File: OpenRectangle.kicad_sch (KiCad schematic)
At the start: 51 parts, among them J1 USB C Connector, J2 JTAG_TC2030, SW1 Boot, U1 XC6206, U2 USBLC6-2SC6, U3 RP2040, U4 W25Q128JVS, Y1 12MHz

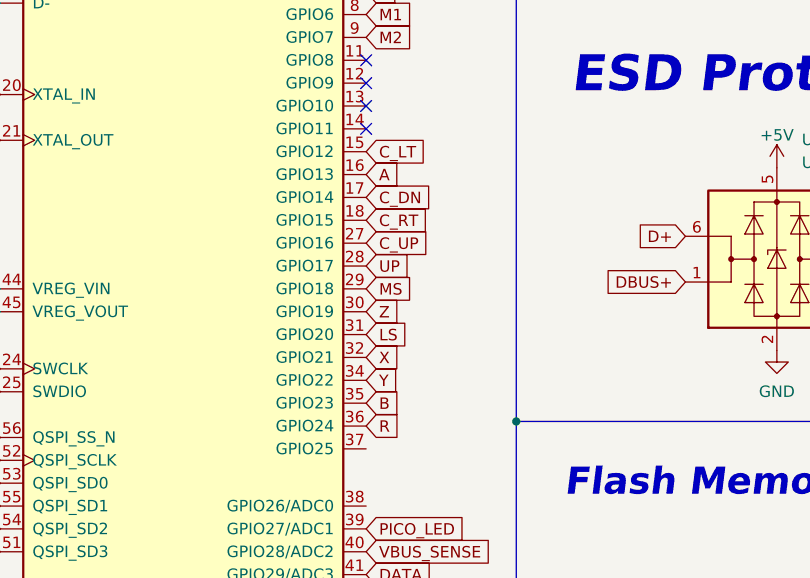
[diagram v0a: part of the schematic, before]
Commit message: modified OpenRectangle design
Modified OpenRectangle design to make it smaller and change button positions
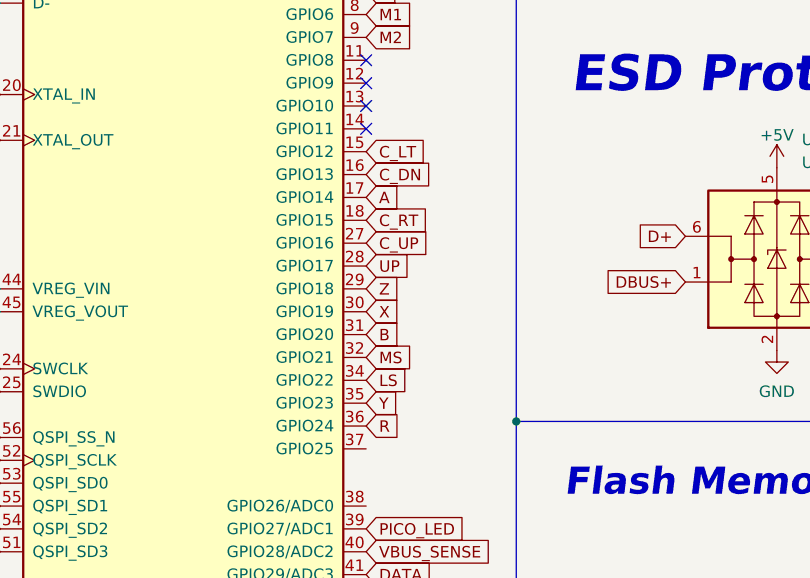
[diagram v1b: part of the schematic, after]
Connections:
- net A: now also U3.17 (GPIO14); no longer U3.16 (GPIO13)
- net B: now also U3.31 (GPIO20); no longer U3.35 (GPIO23)
- net C_DN: now also U3.16 (GPIO13); no longer U3.17 (GPIO14)
- net LS: now also U3.34 (GPIO22); no longer U3.31 (GPIO20)
- net MS: now also U3.32 (GPIO21); no longer U3.29 (GPIO18)
- net X: now also U3.30 (GPIO19); no longer U3.32 (GPIO21)
- net Y: now also U3.35 (GPIO23); no longer U3.34 (GPIO22)
- net Z: now also U3.29 (GPIO18); no longer U3.30 (GPIO19)
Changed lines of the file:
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@@
     )
   )
-  (global_label "Y" (shape input) (at 71.9648 104.394 0) (fields_autoplaced)
-    (effects (font (size 1.27 1.27)) (justify left))
-    (property "Intersheetrefs" "${INTERSHEET_REFS}" (at 75.4665 104.3146 0)
+  (global_label "Y" (shape input) (at 71.9648 106.934 0) (fields_autoplaced)
+    (effects (font (size 1.27 1.27)) (justify left))
+    (property "Intersheetrefs" "${INTERSHEET_REFS}" (at 75.4665 106.8546 0)
       (effects (font (size 1.27 1.27)) (justify left) hide)
     )
@@
     )
   )
-  (global_label "C_DN" (shape input) (at 71.9648 84.074 0) (fields_autoplaced)
-    (effects (font (size 1.27 1.27)) (justify left))
-    (property "Intersheetrefs" "${INTERSHEET_REFS}" (at 79.216 83.9946 0)
+  (global_label "C_DN" (shape input) (at 71.9648 81.534 0) (fields_autoplaced)
+    (effects (font (size 1.27 1.27)) (justify left))
+    (property "Intersheetrefs" "${INTERSHEET_REFS}" (at 79.216 81.4546 0)
       (effects (font (size 1.27 1.27)) (justify left) hide)
     )
@@
     )
   )
-  (global_label "Z" (shape input) (at 71.9648 96.774 0) (fields_autoplaced)
+  (global_label "Z" (shape input) (at 71.9648 94.234 0) (fields_autoplaced)
+    (effects (font (size 1.27 1.27)) (justify left))
+    (property "Intersheetrefs" "${INTERSHEET_REFS}" (at 75.5874 94.1546 0)
+      (effects (font (size 1.27 1.27)) (justify left) hide)
+    )
+  )
+  (global_label "~{RESET}" (shape input) (at 25.8891 48.514 180) (fields_autoplaced)
+    (effects (font (size 1.27 1.27)) (justify right))
+    (property "Intersheetrefs" "${INTERSHEET_REFS}" (at 17.7308 48.4346 0)
+      (effects (font (size 1.27 1.27)) (justify right) hide)
+    )
+  )
+  (global_label "~{RESET}" (shape input) (at 155.702 177.546 180) (fields_autoplaced)
+    (effects (font (size 1.27 1.27)) (justify right))
+    (property "Intersheetrefs" "${INTERSHEET_REFS}" (at 147.5437 177.6254 0)
+      (effects (font (size 1.27 1.27)) (justify right) hide)
+    )
+  )
+  (global_label "XTAL_OUT" (shape input) (at 31.3248 77.724 180) (fields_autoplaced)
+    (effects (font (size 1.27 1.27)) (justify right))
+    (property "Intersheetrefs" "${INTERSHEET_REFS}" (at 20.0217 77.6446 0)
+      (effects (font (size 1.27 1.27)) (justify right) hide)
+    )
+  )
+  (global_label "SD1" (shape input) (at 31.3248 118.364 180) (fields_autoplaced)
+    (effects (font (size 1.27 1.27)) (justify right))
+    (property "Intersheetrefs" "${INTERSHEET_REFS}" (at 25.2227 118.2846 0)
+      (effects (font (size 1.27 1.27)) (justify right) hide)
+    )
+  )
+  (global_label "VBUS_SENSE" (shape input) (at 207.5942 151.384 0) (fields_autoplaced)
+    (effects (font (size 1.27 1.27)) (justify left))
+    (property "Intersheetrefs" "${INTERSHEET_REFS}" (at 222.4137 151.384 0)
+      (effects (font (size 1.27 1.27)) (justify left) hide)
+    )
+  )
+  (global_label "SWCLK" (shape input) (at 155.702 180.086 180) (fields_autoplaced)
+    (effects (font (size 1.27 1.27)) (justify right))
+    (property "Intersheetrefs" "${INTERSHEET_REFS}" (at 147.0599 180.1654 0)
+      (effects (font (size 1.27 1.27)) (justify right) hide)
+    )
+  )
+  (global_label "X" (shape input) (at 71.9648 96.774 0) (fields_autoplaced)
     (effects (font (size 1.27 1.27)) (justify left))
     (property "Intersheetrefs" "${INTERSHEET_REFS}" (at 75.5874 96.6946 0)
@@
     )
   )
-  (global_label "~{RESET}" (shape input) (at 25.8891 48.514 180) (fields_autoplaced)
-    (effects (font (size 1.27 1.27)) (justify right))
-    (property "Intersheetrefs" "${INTERSHEET_REFS}" (at 17.7308 48.4346 0)
-      (effects (font (size 1.27 1.27)) (justify right) hide)
-    )
-  )
-  (global_label "~{RESET}" (shape input) (at 155.702 177.546 180) (fields_autoplaced)
-    (effects (font (size 1.27 1.27)) (justify right))
-    (property "Intersheetrefs" "${INTERSHEET_REFS}" (at 147.5437 177.6254 0)
-      (effects (font (size 1.27 1.27)) (justify right) hide)
-    )
-  )
-  (global_label "XTAL_OUT" (shape input) (at 31.3248 77.724 180) (fields_autoplaced)
-    (effects (font (size 1.27 1.27)) (justify right))
-    (property "Intersheetrefs" "${INTERSHEET_REFS}" (at 20.0217 77.6446 0)
-      (effects (font (size 1.27 1.27)) (justify right) hide)
-    )
-  )
-  (global_label "SD1" (shape input) (at 31.3248 118.364 180) (fields_autoplaced)
-    (effects (font (size 1.27 1.27)) (justify right))
-    (property "Intersheetrefs" "${INTERSHEET_REFS}" (at 25.2227 118.2846 0)
-      (effects (font (size 1.27 1.27)) (justify right) hide)
-    )
-  )
-  (global_label "VBUS_SENSE" (shape input) (at 207.5942 151.384 0) (fields_autoplaced)
-    (effects (font (size 1.27 1.27)) (justify left))
-    (property "Intersheetrefs" "${INTERSHEET_REFS}" (at 222.4137 151.384 0)
-      (effects (font (size 1.27 1.27)) (justify left) hide)
-    )
-  )
-  (global_label "SWCLK" (shape input) (at 155.702 180.086 180) (fields_autoplaced)
-    (effects (font (size 1.27 1.27)) (justify right))
-    (property "Intersheetrefs" "${INTERSHEET_REFS}" (at 147.0599 180.1654 0)
-      (effects (font (size 1.27 1.27)) (justify right) hide)
-    )
-  )
-  (global_label "X" (shape input) (at 71.9648 101.854 0) (fields_autoplaced)
-    (effects (font (size 1.27 1.27)) (justify left))
-    (property "Intersheetrefs" "${INTERSHEET_REFS}" (at 75.5874 101.7746 0)
-      (effects (font (size 1.27 1.27)) (justify left) hide)
-    )
-  )
-  (global_label "A" (shape input) (at 71.9648 81.534 0) (fields_autoplaced)
-    (effects (font (size 1.27 1.27)) (justify left))
-    (property "Intersheetrefs" "${INTERSHEET_REFS}" (at 75.4665 81.4546 0)
+  (global_label "A" (shape input) (at 71.9648 84.074 0) (fields_autoplaced)
+    (effects (font (size 1.27 1.27)) (justify left))
+    (property "Intersheetrefs" "${INTERSHEET_REFS}" (at 75.4665 83.9946 0)
       (effects (font (size 1.27 1.27)) (justify left) hide)
     )
@@
     )
   )
-  (global_label "LS" (shape input) (at 71.9648 99.314 0) (fields_autoplaced)
-    (effects (font (size 1.27 1.27)) (justify left))
-    (property "Intersheetrefs" "${INTERSHEET_REFS}" (at 76.6155 99.2346 0)
+  (global_label "LS" (shape input) (at 71.9648 104.394 0) (fields_autoplaced)
+    (effects (font (size 1.27 1.27)) (justify left))
+    (property "Intersheetrefs" "${INTERSHEET_REFS}" (at 76.6155 104.3146 0)
       (effects (font (size 1.27 1.27)) (justify left) hide)
     )
@@
     )
   )
-  (global_label "MS" (shape input) (at 71.9648 94.234 0) (fields_autoplaced)
-    (effects (font (size 1.27 1.27)) (justify left))
-    (property "Intersheetrefs" "${INTERSHEET_REFS}" (at 77.0389 94.1546 0)
+  (global_label "MS" (shape input) (at 71.9648 101.854 0) (fields_autoplaced)
+    (effects (font (size 1.27 1.27)) (justify left))
+    (property "Intersheetrefs" "${INTERSHEET_REFS}" (at 77.0389 101.7746 0)
       (effects (font (size 1.27 1.27)) (justify left) hide)
     )
@@
     )
   )
-  (global_label "B" (shape input) (at 71.9648 106.934 0) (fields_autoplaced)
-    (effects (font (size 1.27 1.27)) (justify left))
-    (property "Intersheetrefs" "${INTERSHEET_REFS}" (at 75.6479 106.8546 0)
-      (effects (font (size 1.27 1.27)) (justify left) hide)
-    )
+  (global_label "B" (shape input) (at 71.9648 99.314 0) (fields_autoplaced)
+    (effects (font (size 1.27 1.27)) (justify left))
+    (property "Intersheetrefs" "${INTERSHEET_REFS}" (at 75.6479 99.2346 0)
+      (effects (font (size 1.27 1.27)) (justify left) hide)
+    )

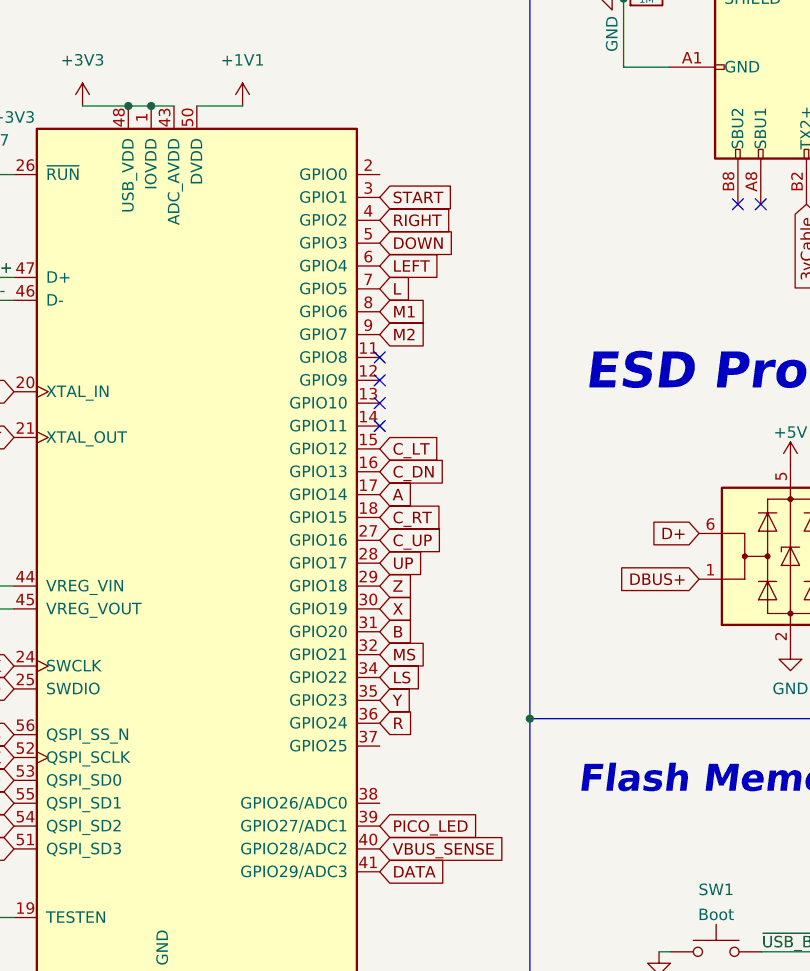
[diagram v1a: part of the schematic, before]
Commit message: Added optional buttons
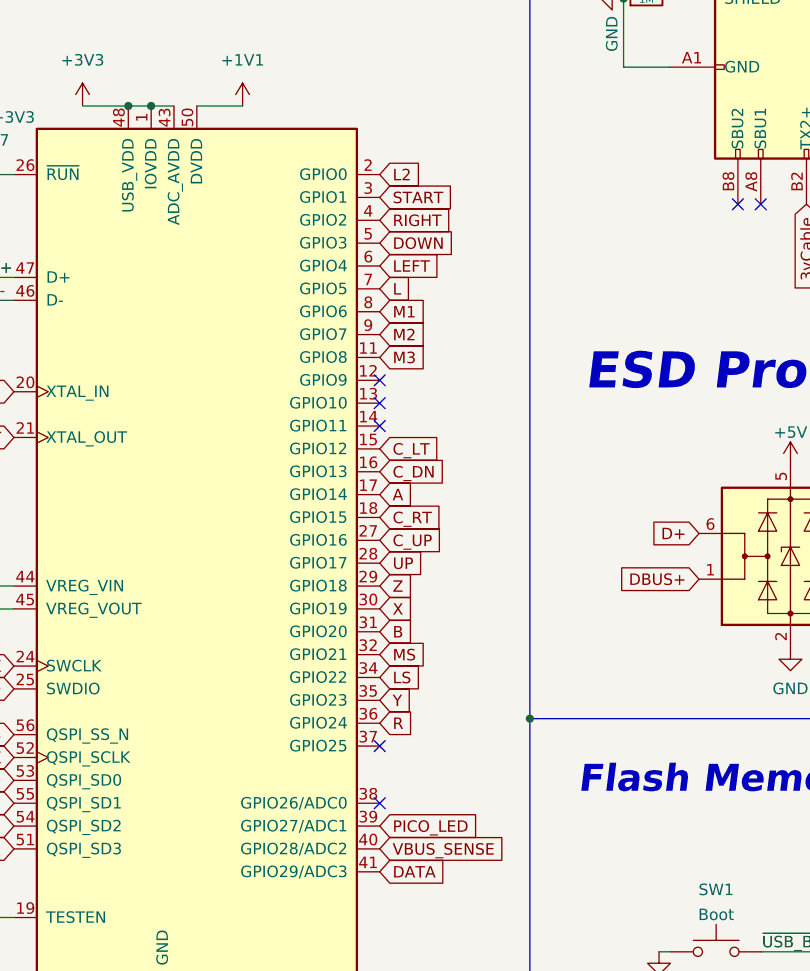
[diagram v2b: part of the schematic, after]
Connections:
- net M3: now reaches U3.11 (GPIO8)
- net L2: now reaches U3.2 (GPIO0)
- no-connect marks 9 -> 10
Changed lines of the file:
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@@
   (junction (at 65.786 180.34) (diameter 0) (color 0 0 0 0)
   )
-  (no_connect (at 71.9648 68.834))
+  (no_connect (at 71.9648 118.364))
+  (no_connect (at 71.9648 112.014))
   (no_connect (at 71.9648 71.374))
   (no_connect (at 71.9648 73.914))
@@
     )
   )
+  (global_label "L2" (shape input) (at 71.9648 48.514 0) (fields_autoplaced)
+    (effects (font (size 1.27 1.27)) (justify left))
+    (property "Intersheetrefs" "${INTERSHEET_REFS}" (at 77.1082 48.514 0)
+      (effects (font (size 1.27 1.27)) (justify left) hide)
+    )
+  )
   (global_label "C_DN" (shape input) (at 71.9648 81.534 0) (fields_autoplaced)
     (effects (font (size 1.27 1.27)) (justify left))
@@
     )
   )
+  (global_label "M3" (shape input) (at 71.9648 68.834 0) (fields_autoplaced)
+    (effects (font (size 1.27 1.27)) (justify left))
+    (property "Intersheetrefs" "${INTERSHEET_REFS}" (at 77.5315 68.834 0)
+      (effects (font (size 1.27 1.27)) (justify left) hide)
+    )
+  )

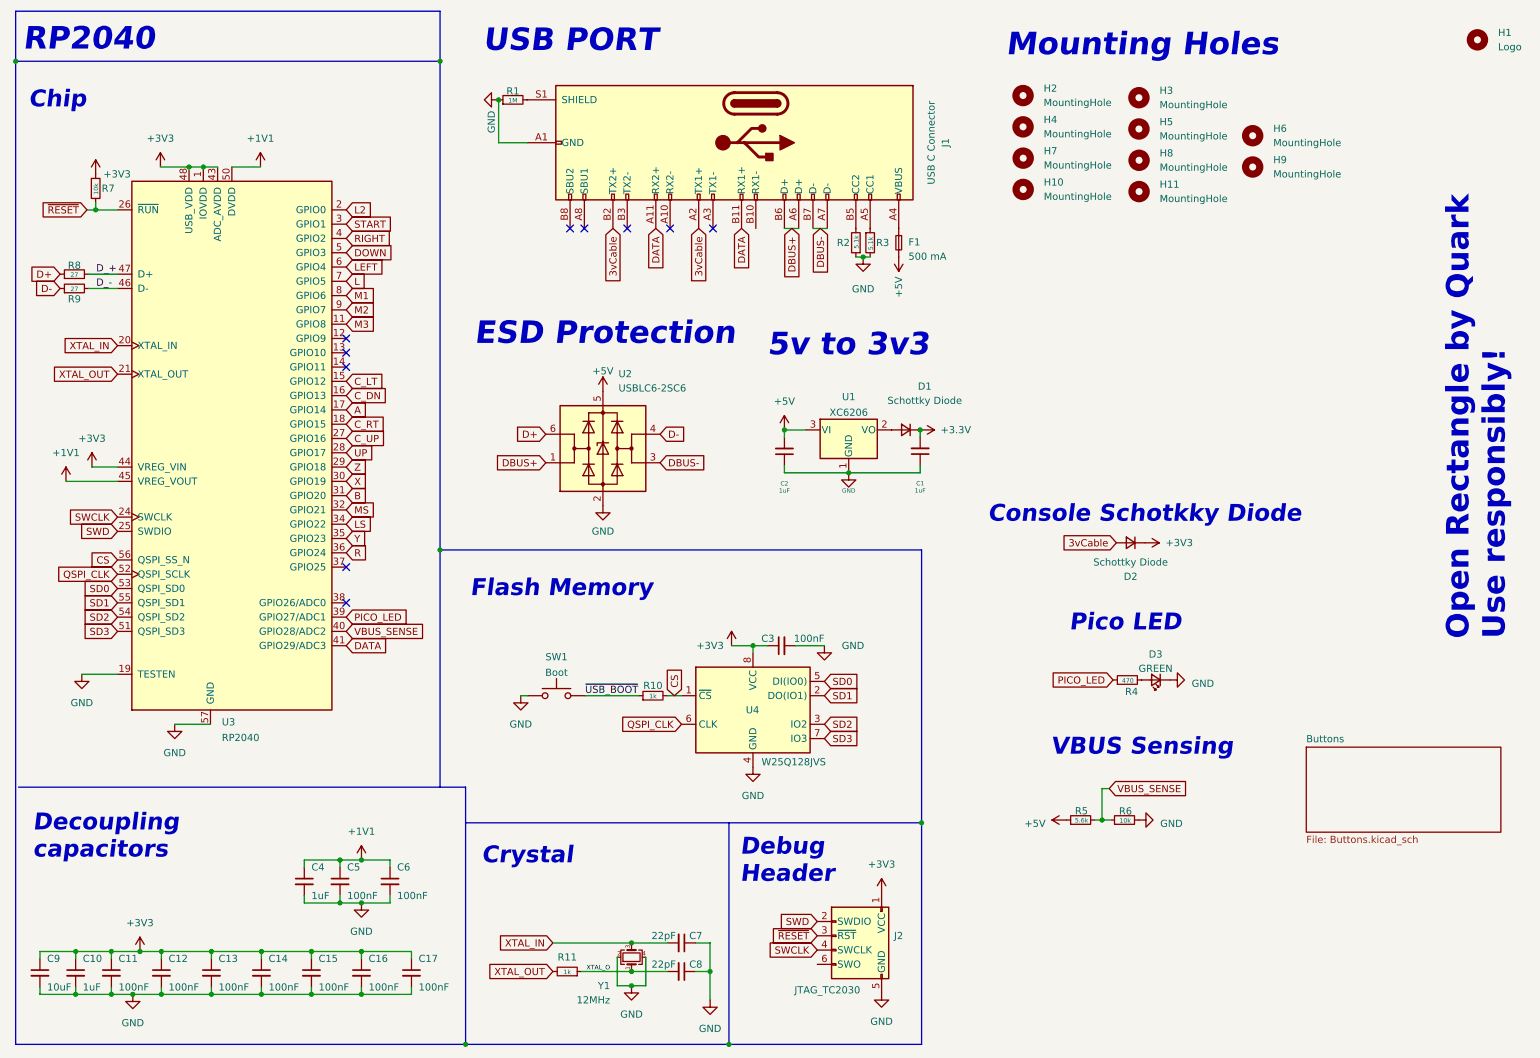
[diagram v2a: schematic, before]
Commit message: updated pinout to default haybox and revised case
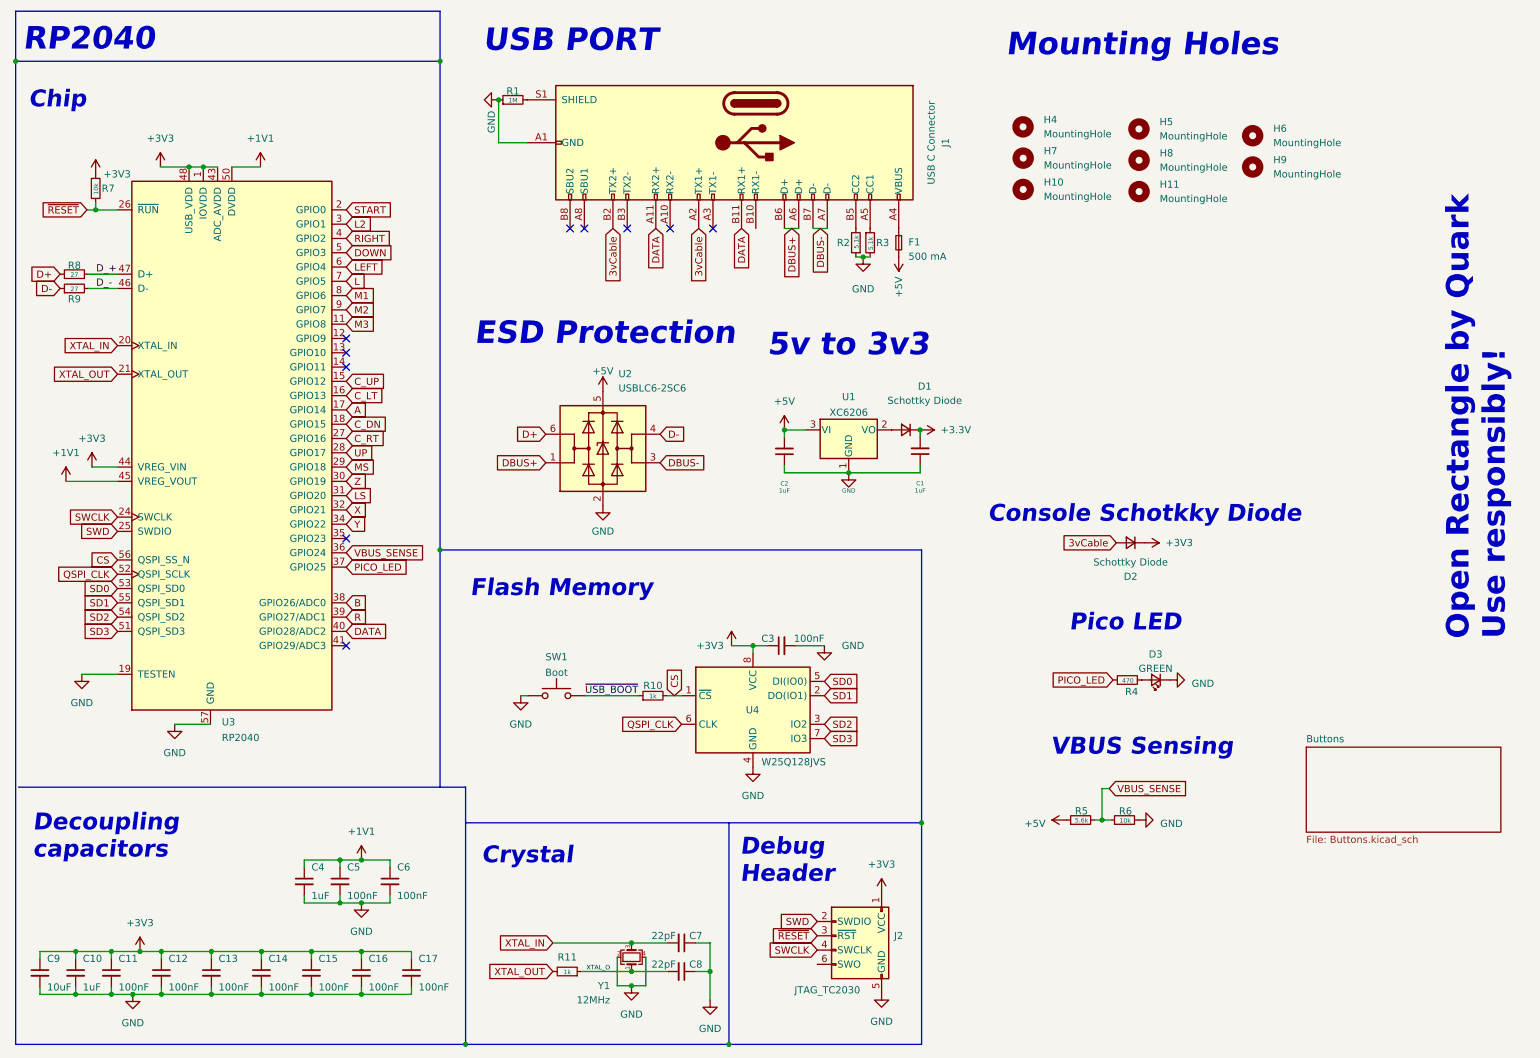
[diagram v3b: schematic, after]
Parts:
- removed H1: Logo, qw-logo:qw new logo mask md, symbol Mechanical:MountingHole
- removed H2, H3: MountingHole, MountingHole:MountingHole_2.2mm_M2_ISO14580_Pad, symbol Mechanical:MountingHole
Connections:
- net B: now also U3.38 (GPIO26/ADC0); no longer U3.31 (GPIO20)
- net C_DN: now also U3.18 (GPIO15); no longer U3.16 (GPIO13)
- net C_LT: now also U3.16 (GPIO13); no longer U3.15 (GPIO12)
- net C_RT: now also U3.27 (GPIO16); no longer U3.18 (GPIO15)
- net C_UP: now also U3.15 (GPIO12); no longer U3.27 (GPIO16)
- net DATA: now also U3.40 (GPIO28/ADC2); no longer U3.41 (GPIO29/ADC3)
- net L2: now also U3.3 (GPIO1); no longer U3.2 (GPIO0)
- net LS: now also U3.31 (GPIO20); no longer U3.34 (GPIO22)
- net MS: now also U3.29 (GPIO18); no longer U3.32 (GPIO21)
- net PICO_LED: now also U3.37 (GPIO25); no longer U3.39 (GPIO27/ADC1)
- net R: now also U3.39 (GPIO27/ADC1); no longer U3.36 (GPIO24)
- net START: now also U3.2 (GPIO0); no longer U3.3 (GPIO1)
- net VBUS_SENSE: now also U3.36 (GPIO24); no longer U3.40 (GPIO28/ADC2)
- net X: now also U3.32 (GPIO21); no longer U3.30 (GPIO19)
- net Y: now also U3.34 (GPIO22); no longer U3.35 (GPIO23)
- net Z: now also U3.30 (GPIO19); no longer U3.29 (GPIO18)
